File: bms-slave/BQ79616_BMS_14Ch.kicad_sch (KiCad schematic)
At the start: 180 parts, among them J1 Conn_Therm, J2 Conn_02x10_Odd_Even, J3 Conn_02x10_Odd_Even, J4 BMS_A_OUT, J5 BMS_A_IN, Q1 MMBT5551, Q10 DMN2024UQ, Q11 DMN2024UQ, Q12 DMN2024UQ, Q13 DMN2024UQ, Q14 DMN2024UQ, Q15 DMN2024UQ, Q2 DMN2024UQ, Q3 DMN2024UQ, Q4 DMN2024UQ, Q5 DMN2024UQ, Q6 DMN2024UQ, Q7 DMN2024UQ, Q8 DMN2024UQ, Q9 DMN2024UQ

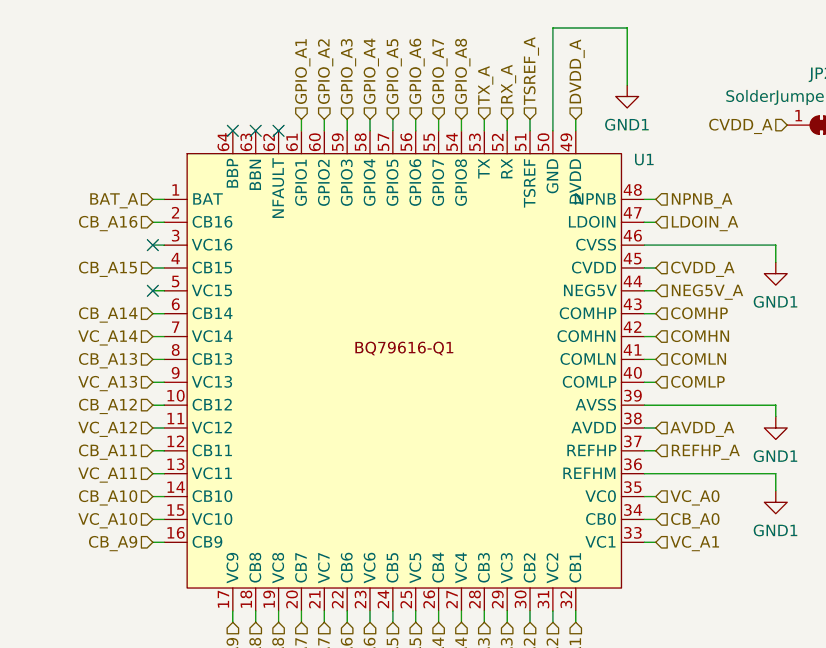
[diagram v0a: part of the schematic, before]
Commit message: Reconfigure file structure and create share lib and 3D CAD
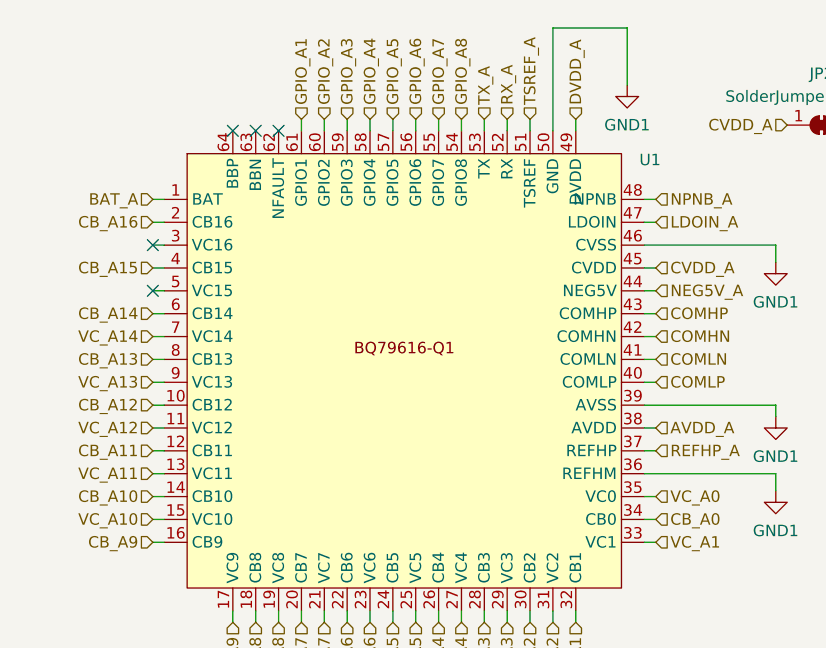
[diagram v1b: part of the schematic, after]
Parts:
- removed U1: ~, Package_QFP:HTQFP-64-1EP_10x10mm_P0.5mm_EP8x8mm, symbol (1)New_Library:BQ_79616
- added U1: ~, Package_QFP:HTQFP-64-1EP_10x10mm_P0.5mm_EP8x8mm, symbol Project_Lib:BQ79616-Q1
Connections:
- net AVDD_A: now also U1.38 (AVDD)
- net BAT_A: now also U1.1 (BAT), U1.2 (CB16), U1.4 (CB15), U1.6 (CB14)
- net CB_A0: now also U1.34 (CB0)
- net CB_A1: now also U1.32 (CB1)
- net CB_A10: now also U1.14 (CB10)
- net CB_A11: now also U1.12 (CB11)
- net CB_A12: now also U1.10 (CB12)
- net CB_A13: now also U1.8 (CB13)
- net CB_A2: now also U1.30 (CB2)
- net CB_A3: now also U1.28 (CB3)
- net CB_A4: now also U1.26 (CB4)
- net CB_A5: now also U1.24 (CB5)
- net CB_A6: now also U1.22 (CB6)
- net CB_A7: now also U1.20 (CB7)
- net CB_A8: now also U1.18 (CB8)
- net CB_A9: now also U1.16 (CB9)
- net COMHN: now also U1.42 (COMHN)
- net COMHP: now also U1.43 (COMHP)
- net COMLN: now also U1.41 (COMLN)
- net COMLP: now also U1.40 (COMLP)
- net CVDD_A: now also U1.45 (CVDD)
- net DVDD_A: now also U1.49 (DVDD)
- net GND1: now also U1.36 (REFHM), U1.39 (AVSS), U1.46 (CVSS), U1.50 (GND)
- net GPIO_A1: now also U1.61 (GPIO1)
- net GPIO_A2: now also U1.60 (GPIO2)
- net GPIO_A3: now also U1.59 (GPIO3)
- net GPIO_A4: now also U1.58 (GPIO4)
- net GPIO_A5: now also U1.57 (GPIO5)
- net GPIO_A6: now also U1.56 (GPIO6)
- net GPIO_A7: now also U1.55 (GPIO7)
- net GPIO_A8: now also U1.54 (GPIO8)
- net LDOIN_A: now also U1.47 (LDOIN)
- net NEG5V_A: now also U1.44 (NEG5V)
- net NPNB_A: now also U1.48 (NPNB)
- net REFHP_A: now also U1.37 (REFHP)
- net RX_A: now also U1.52 (RX)
- net TSREF_A: now also U1.51 (TSREF)
- net TX_A: now also U1.53 (TX)
- net VC_A0: now also U1.35 (VC0)
- net VC_A1: now also U1.33 (VC1)
- net VC_A10: now also U1.15 (VC10)
- net VC_A11: now also U1.13 (VC11)
- net VC_A12: now also U1.11 (VC12)
- net VC_A13: now also U1.9 (VC13)
- net VC_A14: now also U1.7 (VC14)
- net VC_A2: now also U1.31 (VC2)
- net VC_A3: now also U1.29 (VC3)
- net VC_A4: now also U1.27 (VC4)
- net VC_A5: now also U1.25 (VC5)
- net VC_A6: now also U1.23 (VC6)
- net VC_A7: now also U1.21 (VC7)
- net VC_A8: now also U1.19 (VC8)
- net VC_A9: now also U1.17 (VC9)
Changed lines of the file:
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@@
-    )
-  )
-  (symbol (lib_id "(1)New_Library:BQ_79616") (at 147.955 54.61 0) (unit 1)
-    (in_bom yes) (on_board yes) (dnp no) (fields_autoplaced)
-    (property "Reference" "U1" (at 174.625 31.1719 0)
-      (effects (font (size 1.27 1.27)))
-    )
-    (property "Value" "~" (at 123.825 50.8 0)
-      (effects (font (size 1.27 1.27)))
-    )
-    (property "Footprint" "Package_QFP:HTQFP-64-1EP_10x10mm_P0.5mm_EP8x8mm" (at 123.825 50.8 0)
-      (effects (font (size 1.27 1.27)) hide)
-    )
-    (property "Datasheet" "" (at 123.825 50.8 0)
-      (effects (font (size 1.27 1.27)) hide)
-    )
-    (pin "38")
-    (pin "47")
-    (pin "7")
-    (pin "30")
-    (pin "24")
-    (pin "27")
-    (pin "23")
-    (pin "13")
-    (pin "16")
-    (pin "18")
-    (pin "2")
-    (pin "29")
-    (pin "12")
-    (pin "14")
-    (pin "48")
-    (pin "15")
-    (pin "31")
-    (pin "43")
-    (pin "49")
-    (pin "39")
-    (pin "10")
-    (pin "35")
-    (pin "17")
-    (pin "42")
-    (pin "5")
-    (pin "1")
-    (pin "50")
-    (pin "28")
-    (pin "37")
-    (pin "46")
-    (pin "52")
-    (pin "55")
-    (pin "25")
-    (pin "4")
-    (pin "44")
-    (pin "41")
-    (pin "19")
-    (pin "33")
-    (pin "53")
-    (pin "56")
-    (pin "59")
-    (pin "6")
-    (pin "54")
-    (pin "40")
-    (pin "11")
-    (pin "21")
-    (pin "3")
-    (pin "58")
-    (pin "60")
-    (pin "61")
-    (pin "32")
-    (pin "36")
-    (pin "62")
-    (pin "51")
-    (pin "20")
-    (pin "34")
-    (pin "45")
-    (pin "22")
-    (pin "57")
-    (pin "63")
-    (pin "64")
-    (pin "26")
-    (pin "8")
-    (pin "9")
-    (instances
-      (project "BQ79616_BMS_14Ch"
-        (path "/0ff84c0c-cd95-4e37-82ee-50268bd68af4"
-          (reference "U1") (unit 1)
-        )
-      )
     )
   )
@@
         )
       )
+    )
+  )
+  (symbol (lib_id "Project_Lib:BQ79616-Q1") (at 147.955 53.34 0) (unit 1)
+    (in_bom yes) (on_board yes) (dnp no) (fields_autoplaced)
+    (property "Reference" "U1" (at 175.26 31.1719 0)
+      (effects (font (size 1.27 1.27)))
+    )
+    (property "Value" "~" (at 147.955 53.34 0)
+      (effects (font (size 1.27 1.27)))
+    )
+    (property "Footprint" "Package_QFP:HTQFP-64-1EP_10x10mm_P0.5mm_EP8x8mm" (at 147.955 53.34 0)
+      (effects (font (size 1.27 1.27)) hide)
+    )
+    (property "Datasheet" "" (at 147.955 53.34 0)
+      (effects (font (size 1.27 1.27)) hide)
+    )
+    (pin "1")
+    (pin "22")
+    (pin "14")
+    (pin "17")
+    (pin "13")
+    (pin "12")
+    (pin "18")
+    (pin "15")
+    (pin "23")
+    (pin "2")
+    (pin "26")
+    (pin "20")
+    (pin "19")
+    (pin "16")
+    (pin "21")
+    (pin "24")
+    (pin "25")
+    (pin "27")
+    (pin "28")
+    (pin "29")
+    (pin "3")
+    (pin "30")
+    (pin "31")
+    (pin "32")
+    (pin "33")
+    (pin "34")
+    (pin "35")
+    (pin "36")
+    (pin "37")
+    (pin "38")
+    (pin "39")
+    (pin "4")
+    (pin "40")
+    (pin "41")
+    (pin "42")
+    (pin "43")
+    (pin "44")
+    (pin "45")
+    (pin "46")
+    (pin "47")
+    (pin "48")
+    (pin "49")
+    (pin "5")
+    (pin "50")
+    (pin "51")
+    (pin "52")
+    (pin "53")
+    (pin "54")
+    (pin "55")
+    (pin "56")
+    (pin "57")
+    (pin "58")
+    (pin "59")
+    (pin "6")
+    (pin "60")
+    (pin "10")
+    (pin "61")
+    (pin "62")
+    (pin "63")
+    (pin "64")
+    (pin "7")
+    (pin "8")
+    (pin "9")
+    (pin "11")
+    (instances
+      (project "BQ79616_BMS_14Ch"
+        (path "/0ff84c0c-cd95-4e37-82ee-50268bd68af4"
+          (reference "U1") (unit 1)
+        )
+      )

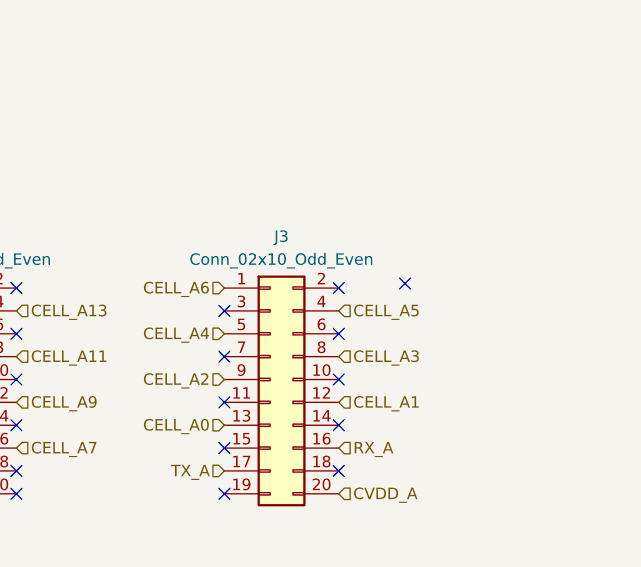
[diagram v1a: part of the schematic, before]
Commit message: Finish slave basic layout, will be tweaked later on
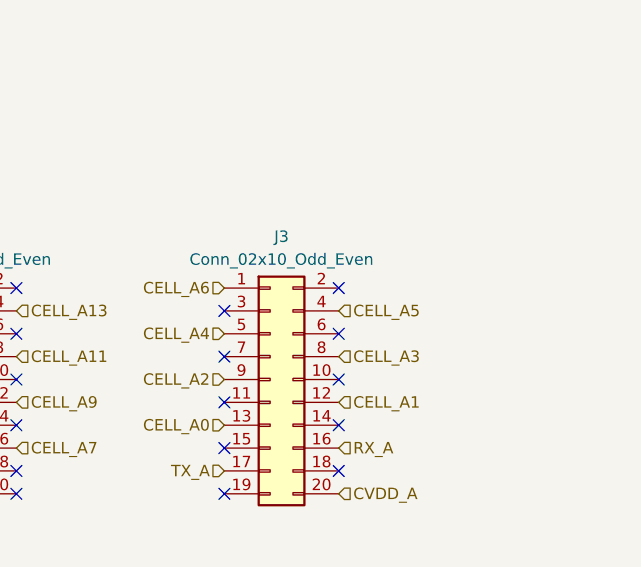
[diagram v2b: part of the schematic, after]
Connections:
- no-connect marks 33 -> 32
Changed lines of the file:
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@@
   (no_connect (at 225.044 48.26))
   (no_connect (at 205.105 126.365))
-  (no_connect (at 268.224 47.752))
   (no_connect (at 225.044 53.34))
   (no_connect (at 212.344 71.12))

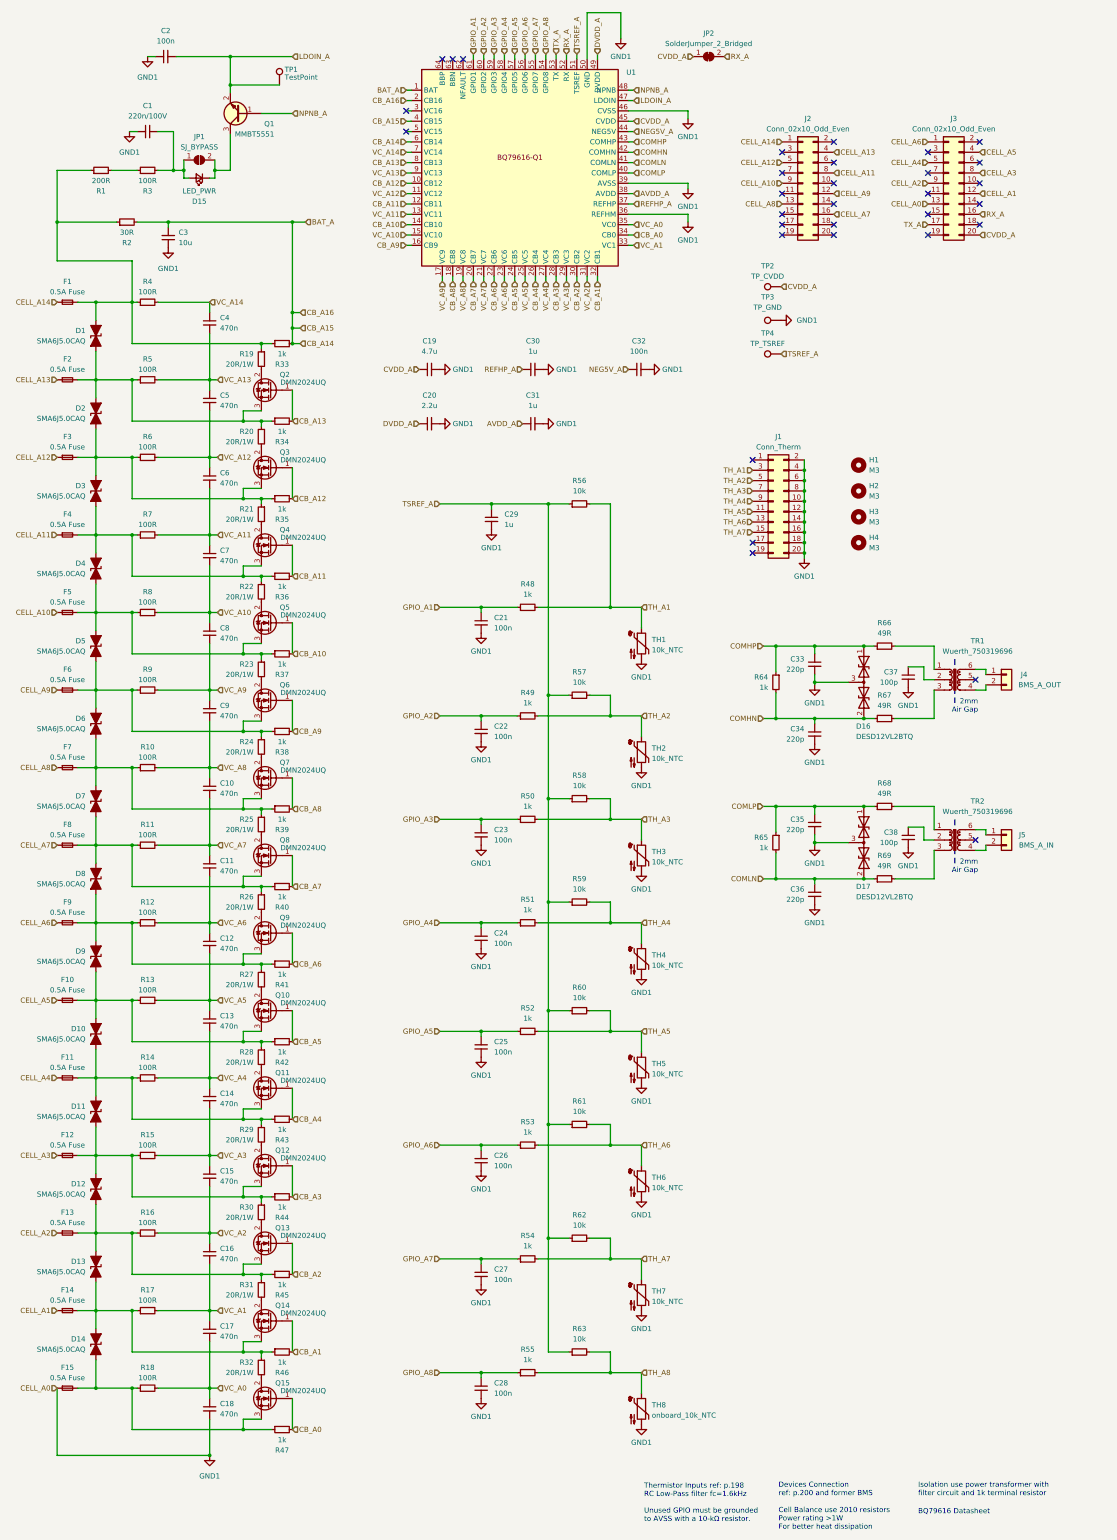
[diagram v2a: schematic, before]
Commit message: feat: improve bms thermal performance
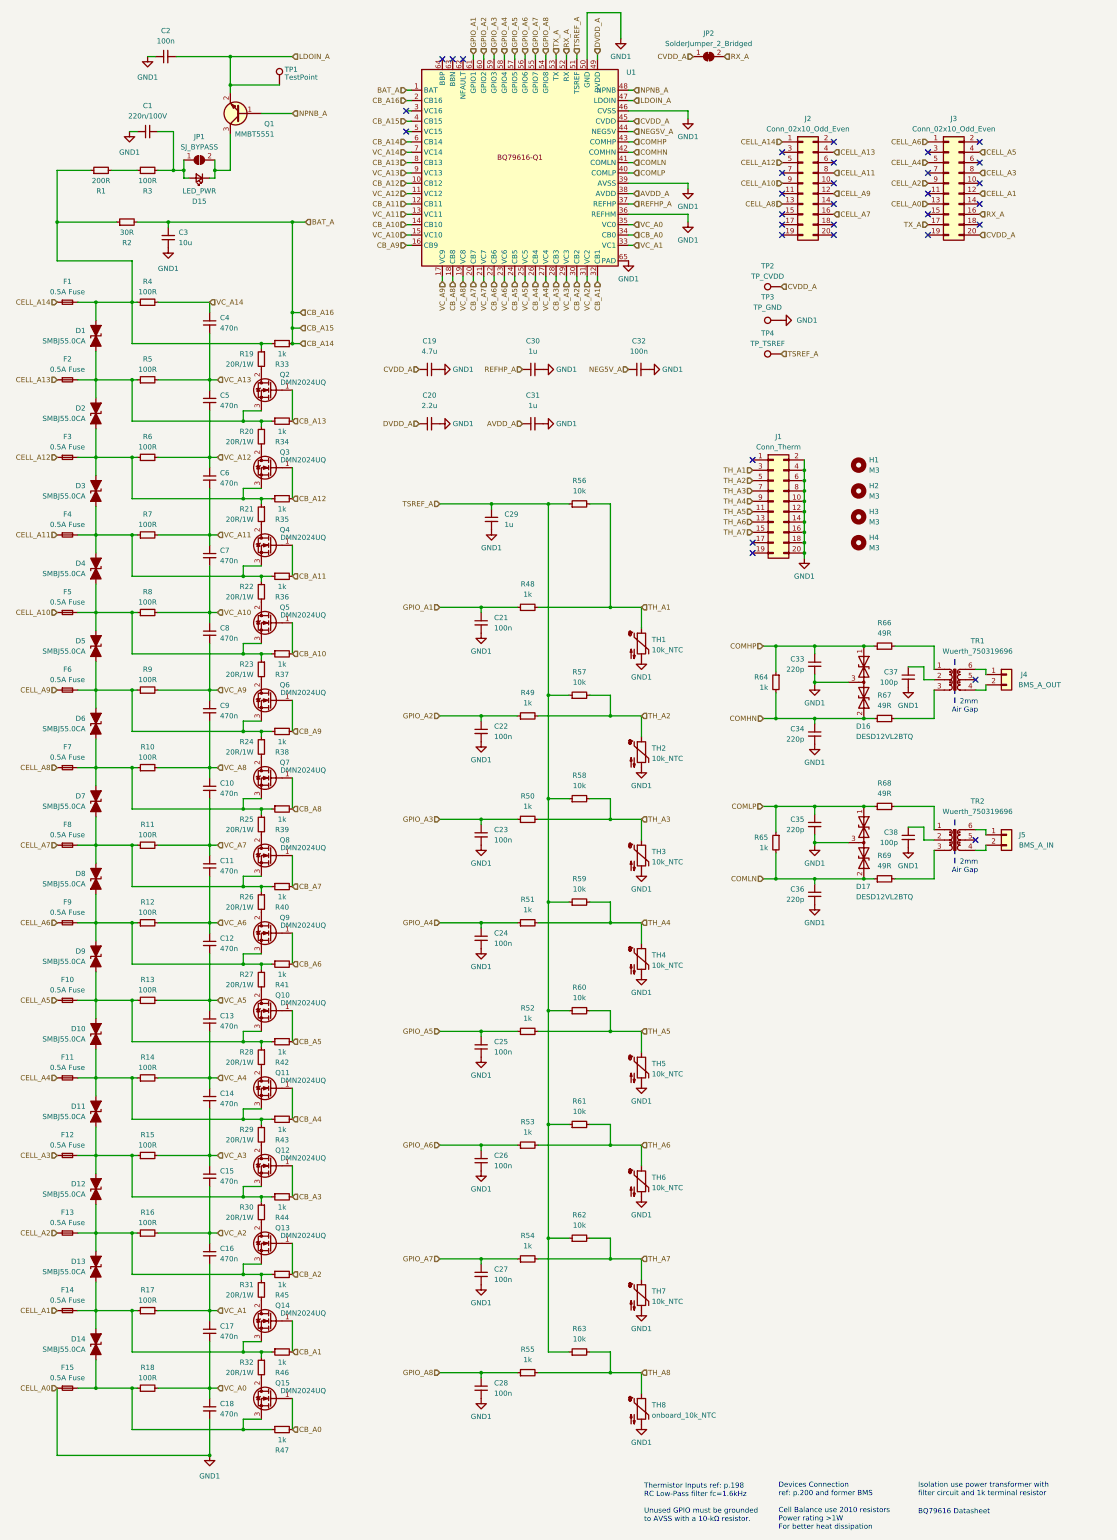
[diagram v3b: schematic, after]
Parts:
- D1, D10, D11, D12, D13, D14, D2, D3, D4, D5, D6, D7, D8, D9: value SMA6J5.0CAQ -> SMBJ55.0CA; footprint Diode_SMD:D_SMA -> Diode_SMD:D_SMB
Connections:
- net GND1: now also U1.65 (PAD)

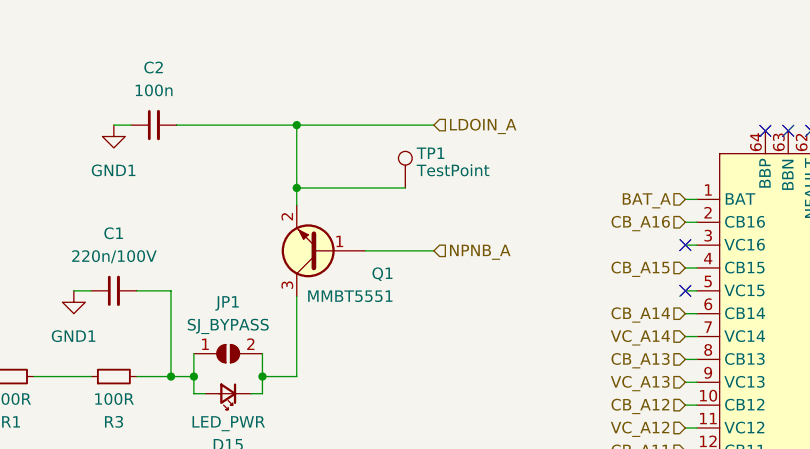
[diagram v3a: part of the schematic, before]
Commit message: fix: improve GND plant
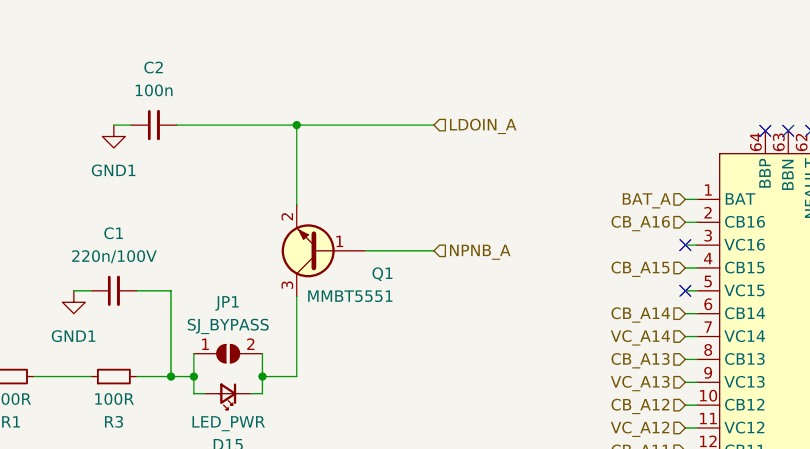
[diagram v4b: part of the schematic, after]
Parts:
- removed TP1: TestPoint, TestPoint:TestPoint_THTPad_D1.0mm_Drill0.5mm, symbol Connector:TestPoint
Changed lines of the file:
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@@
   (junction (at 170.18 266.7) (diameter 0) (color 0 0 0 0)
   )
-  (junction (at 76.835 34.29) (diameter 0) (color 0 0 0 0)
-  )
   (junction (at 84.455 326.39) (diameter 0) (color 0 0 0 0)
   )
@@
     (stroke (width 0) (type default))
   )
-  (wire (pts (xy 76.835 34.29) (xy 88.9 34.29))
-    (stroke (width 0) (type default))
-  )
   (wire (pts (xy 71.755 182.88) (xy 71.755 185.42))
     (stroke (width 0) (type default))
@@
     (stroke (width 0) (type default))
   )
-  (wire (pts (xy 76.835 27.305) (xy 76.835 34.29))
+  (wire (pts (xy 76.835 27.305) (xy 76.835 36.195))
     (stroke (width 0) (type default))
   )
@@
     (stroke (width 0) (type default) (color 0 0 255 0.98))
   )
-  (wire (pts (xy 76.835 34.29) (xy 76.835 36.195))
-    (stroke (width 0) (type default))
-  )
   (wire (pts (xy 71.755 228.6) (xy 71.755 240.03))
     (stroke (width 0) (type default))
@@
         )
       )
-    )
-  )
-  (symbol (lib_id "Connector:TestPoint") (at 88.9 34.29 0) (unit 1)
-    (in_bom yes) (on_board yes) (dnp no)
-    (property "Reference" "TP1" (at 90.17 30.48 0)
-      (effects (font (size 1.27 1.27)) (justify left))
-    )
-    (property "Value" "TestPoint" (at 90.17 32.385 0)
-      (effects (font (size 1.27 1.27)) (justify left))
-    )
-    (property "Footprint" "TestPoint:TestPoint_THTPad_D1.0mm_Drill0.5mm" (at 93.98 34.29 0)
-      (effects (font (size 1.27 1.27)) hide)
-    )
-    (property "Datasheet" "~" (at 93.98 34.29 0)
-      (effects (font (size 1.27 1.27)) hide)
-    )
-    (pin "1")
-    (instances
-      (project "BQ79616_BMS_14Ch"
-        (path "/0ff84c0c-cd95-4e37-82ee-50268bd68af4"
-          (reference "TP1") (unit 1)
-        )
-      )
